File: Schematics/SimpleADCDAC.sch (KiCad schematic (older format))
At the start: 65 parts

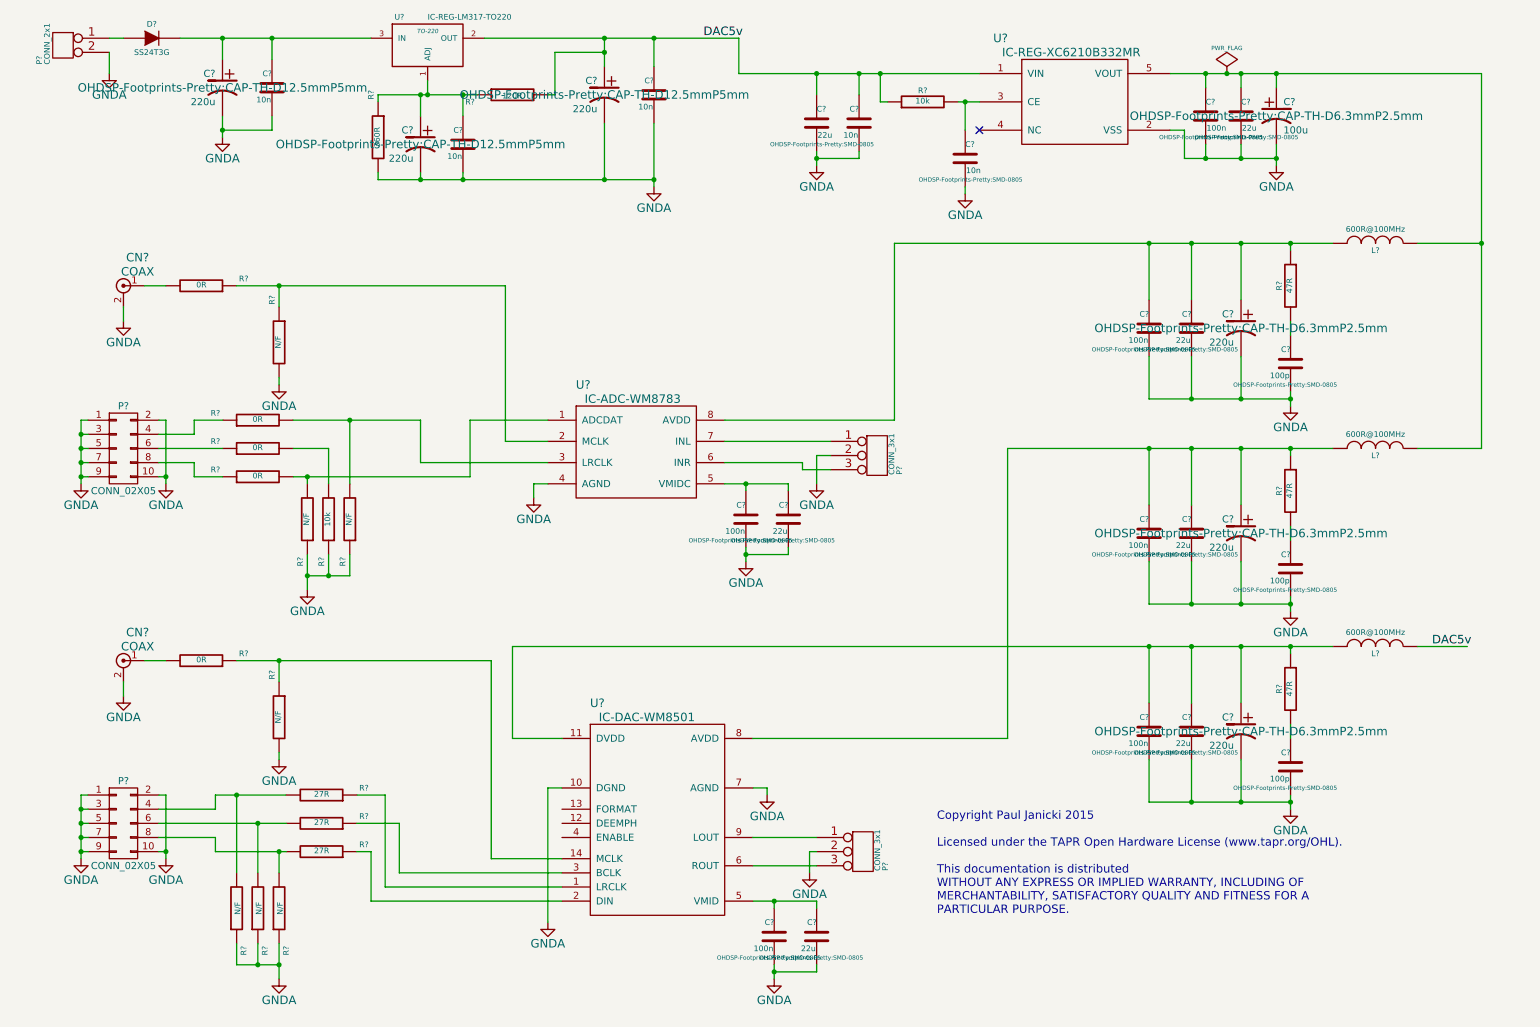
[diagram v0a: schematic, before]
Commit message: Adding ADC/DAC
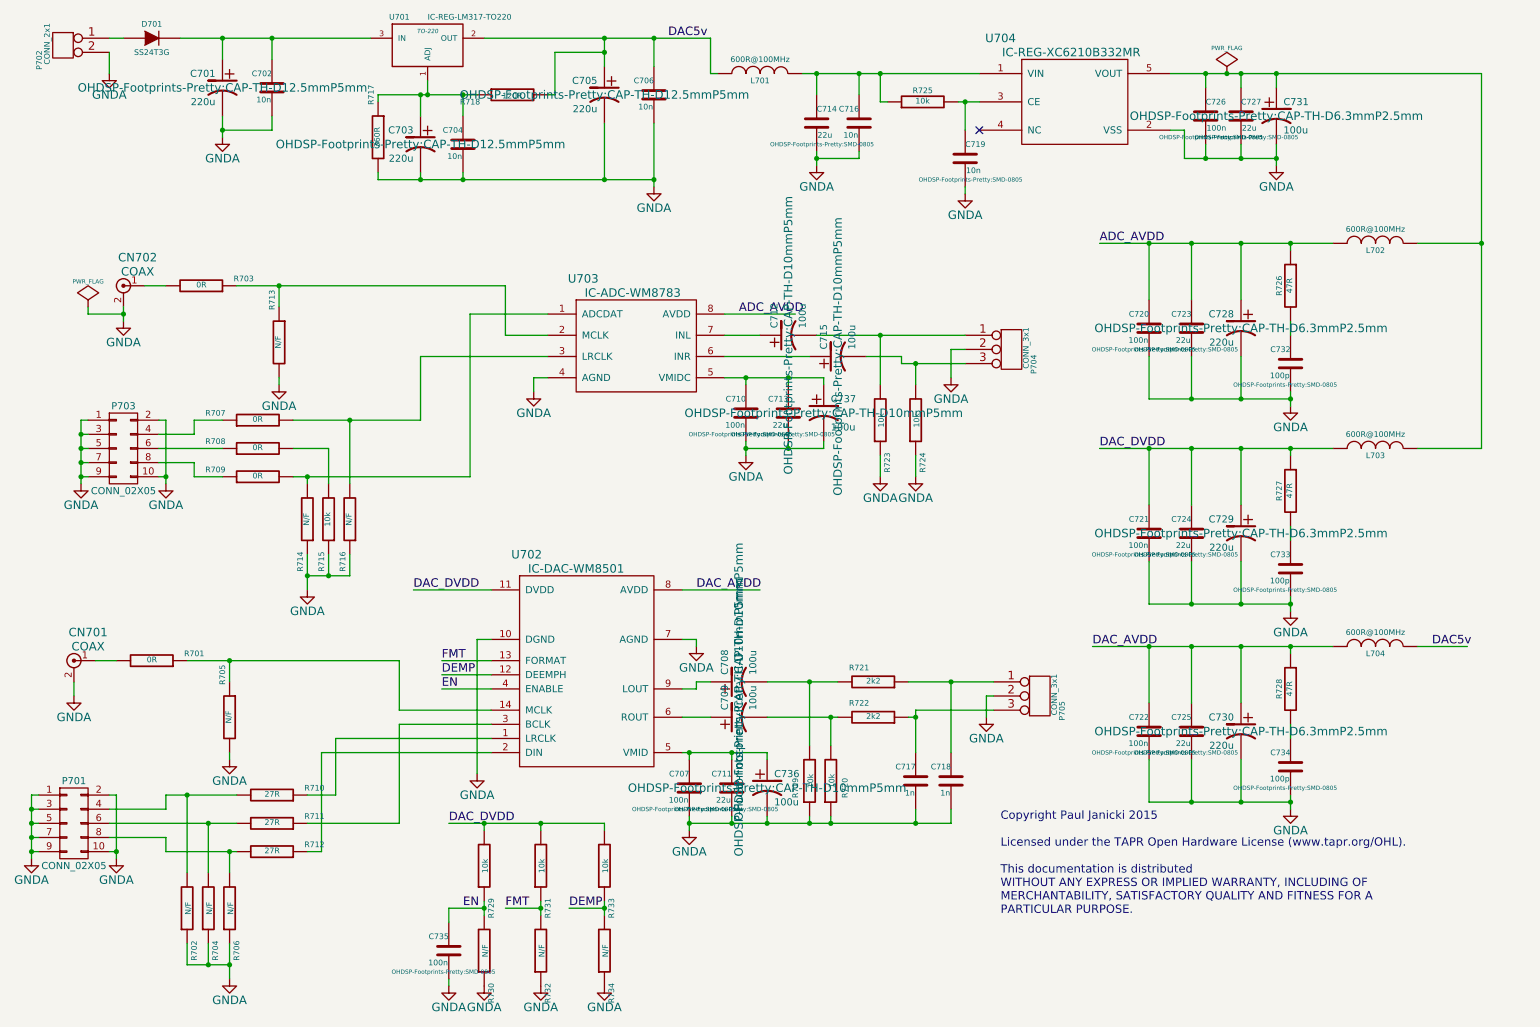
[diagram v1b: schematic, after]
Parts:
- added C708, C709, C712, C715, C736, C737: 100u, OHDSP-Footprints-Pretty:CAP-TH-D10mmP5mm, symbol CP1
- added C717, C718: 1n, symbol C
- added C735: 100n, OHDSP-Footprints-Pretty:SMD-0805, symbol C
- added L701: 600R@100MHz, OHDSP-Footprints-Pretty:SMD-0805, symbol INDUCTOR
- added R719, R720, R723, R724, R729, R731, R733: 10k, OHDSP-Footprints-Pretty:SMD-0603, symbol R
- added R721, R722: 2k2, OHDSP-Footprints-Pretty:SMD-0603, symbol R
- added R730, R732, R734: N/F, OHDSP-Footprints-Pretty:SMD-0603, symbol R
- gave numbers to parts that had none: 65
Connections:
- net DAC5v: now also L701.2; no longer C714.1, C716.1, R725.1, U704.1 (VIN)
- net GNDA: now also C717.2, C718.2, C735.2, C736.2, C737.2, R719.1, R720.1, R723.1, R724.1, R730.1, R732.1, R734.1
- net at C710.1, C713.1, U703.5 (VMIDC): now also C737.1
- net at U703.6 (INR): now also C715.1; no longer P704.3 (P3)
- net at U703.7 (INL): now also C712.1; no longer P704.1 (P1)
- net ADC_AVDD: now reaches C720.1, C723.1, C728.1, L702.2, R726.1, U703.8 (AVDD)
- net DAC_AVDD: now reaches C722.1, C725.1, C730.1, L704.2, R728.1
- net DAC_AVDD: now also U702.8 (AVDD); no longer U702.11 (DVDD)
- net DEMP: now reaches U702.12 (DEEMPH)
- net DEMP: now also R733.1, R734.2
- net FMT: now reaches U702.13 (FORMAT)
- net FMT: now also R731.1, R732.2
- net EN: now reaches U702.4 (ENABLE)
- net EN: now also C735.1, R729.1, R730.2
- net at C707.1, C711.1, U702.5 (VMID): now also C736.1
- net at U702.6 (ROUT): now also C709.1; no longer P705.3 (P3)
- net DAC_DVDD: now reaches C721.1, C724.1, C729.1, L703.2, R727.1
- net DAC_DVDD: now also U702.11 (DVDD), R729.2, R731.2, R733.2; no longer U702.8 (AVDD)
- net at U702.9 (LOUT): now also C708.1; no longer P705.1 (P1)
- new net: C714.1, C716.1, L701.1, R725.1, U704.1 (VIN)
- new net: C708.2, R719.2, R721.2
- new net: C709.2, R720.2, R722.2
- new net: C718.1, P705.1 (P1), R721.1
- new net: C717.1, P705.3 (P3), R722.1
- new net: C712.2, P704.1 (P1), R723.2
- new net: C715.2, P704.3 (P3), R724.2
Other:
- moved on the sheet: C707, C710, C711, C713, CN701, P701, P704, P705, R701, R702, R704, R705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

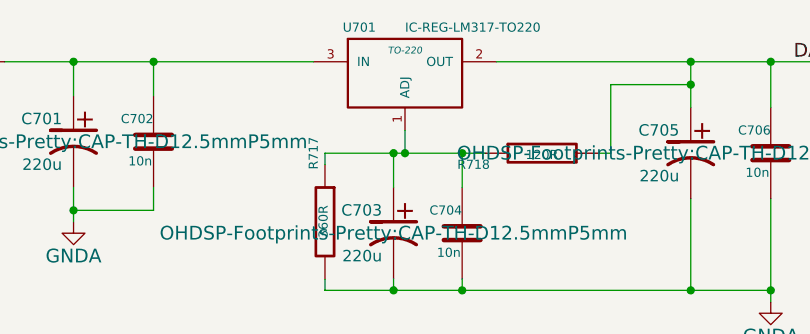
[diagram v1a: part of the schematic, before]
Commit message: Adding DAC/ADC
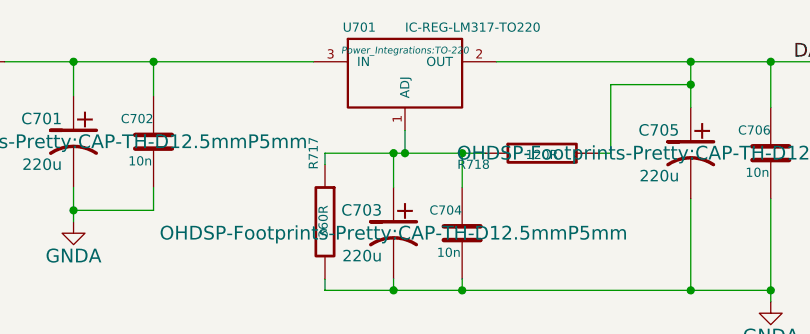
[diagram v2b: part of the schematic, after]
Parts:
- C702, C704, C706, C716, C717, C718: footprint (none) -> OHDSP-Footprints-Pretty:CAP_TH_5mm
- P704, P705: footprint (none) -> OHDSP-Footprints-Pretty:CONN_SIL_3
- R702, R704, R706, R707, R708, R709, R710, R711, R712, R714, R715, R716, R719, R720, R721, R722, R723, R724, R729, R730, R731, R732, R733, R734: footprint OHDSP-Footprints-Pretty:SMD-0603 -> OHDSP-Footprints-Pretty:SMD-0805
- U701: footprint TO-220 -> Power_Integrations:TO-220
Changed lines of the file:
@@
 F 0 "U703" H 4500 3100 60  0000 C CNN
 F 1 "IC-ADC-WM8783" H 4850 3000 60  0000 C CNN
-F 2 "" H 4250 2850 60  0000 C CNN
+F 2 "" H 4250 2850 60  0001 C CNN
 F 3 "" H 4250 2850 60  0000 C CNN
 	1    4250 2850
@@
 F 0 "U702" H 4100 5050 60  0000 C CNN
 F 1 "IC-DAC-WM8501" H 4450 4950 60  0000 C CNN
-F 2 "" H 6250 5150 60  0000 C CNN
+F 2 "" H 6250 5150 60  0001 C CNN
 F 3 "" H 6250 5150 60  0000 C CNN
 	1    3850 4800
@@
 F 0 "R714" V 2600 4600 40  0000 C CNN
 F 1 "N/F" V 2557 4301 40  0000 C CNN
-F 2 "OHDSP-Footprints-Pretty:SMD-0603" V 2480 4300 30  0001 C CNN
+F 2 "OHDSP-Footprints-Pretty:SMD-0805" V 2480 4300 30  0001 C CNN
 F 3 "~" H 2550 4300 30  0000 C CNN
 	1    2550 4300
@@
 F 0 "R715" V 2750 4600 40  0000 C CNN
 F 1 "10k" V 2707 4301 40  0000 C CNN
-F 2 "OHDSP-Footprints-Pretty:SMD-0603" V 2630 4300 30  0001 C CNN
+F 2 "OHDSP-Footprints-Pretty:SMD-0805" V 2630 4300 30  0001 C CNN
 F 3 "~" H 2700 4300 30  0000 C CNN
 	1    2700 4300
@@
 F 0 "R716" V 2900 4600 40  0000 C CNN
 F 1 "N/F" V 2857 4301 40  0000 C CNN
-F 2 "OHDSP-Footprints-Pretty:SMD-0603" V 2780 4300 30  0001 C CNN
+F 2 "OHDSP-Footprints-Pretty:SMD-0805" V 2780 4300 30  0001 C CNN
 F 3 "~" H 2850 4300 30  0000 C CNN
 	1    2850 4300
@@
 F 0 "R707" V 2250 3900 40  0000 C CNN
 F 1 "0R" V 2207 3601 40  0000 C CNN
-F 2 "OHDSP-Footprints-Pretty:SMD-0603" V 2130 3600 30  0001 C CNN
+F 2 "OHDSP-Footprints-Pretty:SMD-0805" V 2130 3600 30  0001 C CNN
 F 3 "~" H 2200 3600 30  0000 C CNN
 	1    2200 3600
@@
 F 0 "R708" V 2250 4100 40  0000 C CNN
 F 1 "0R" V 2207 3801 40  0000 C CNN
-F 2 "OHDSP-Footprints-Pretty:SMD-0603" V 2130 3800 30  0001 C CNN
+F 2 "OHDSP-Footprints-Pretty:SMD-0805" V 2130 3800 30  0001 C CNN
 F 3 "~" H 2200 3800 30  0000 C CNN
 	1    2200 3800
@@
 F 0 "R709" V 2250 4300 40  0000 C CNN
 F 1 "0R" V 2207 4001 40  0000 C CNN
-F 2 "OHDSP-Footprints-Pretty:SMD-0603" V 2130 4000 30  0001 C CNN
+F 2 "OHDSP-Footprints-Pretty:SMD-0805" V 2130 4000 30  0001 C CNN
 F 3 "~" H 2200 4000 30  0000 C CNN
 	1    2200 4000
@@
 F 0 "R710" V 2350 6550 40  0000 C CNN
 F 1 "27R" V 2307 6251 40  0000 C CNN
-F 2 "OHDSP-Footprints-Pretty:SMD-0603" V 2230 6250 30  0001 C CNN
+F 2 "OHDSP-Footprints-Pretty:SMD-0805" V 2230 6250 30  0001 C CNN
 F 3 "~" H 2300 6250 30  0000 C CNN
 	1    2300 6250
@@
 F 0 "R706" V 2050 7350 40  0000 C CNN
 F 1 "N/F" V 2007 7051 40  0000 C CNN
-F 2 "OHDSP-Footprints-Pretty:SMD-0603" V 1930 7050 30  0001 C CNN
+F 2 "OHDSP-Footprints-Pretty:SMD-0805" V 1930 7050 30  0001 C CNN
 F 3 "~" H 2000 7050 30  0000 C CNN
 	1    2000 7050
@@
 F 0 "R704" V 1900 7350 40  0000 C CNN
 F 1 "N/F" V 1857 7051 40  0000 C CNN
-F 2 "OHDSP-Footprints-Pretty:SMD-0603" V 1780 7050 30  0001 C CNN
+F 2 "OHDSP-Footprints-Pretty:SMD-0805" V 1780 7050 30  0001 C CNN
 F 3 "~" H 1850 7050 30  0000 C CNN
 	1    1850 7050
@@
 F 0 "R702" V 1750 7350 40  0000 C CNN
 F 1 "N/F" V 1707 7051 40  0000 C CNN
-F 2 "OHDSP-Footprints-Pretty:SMD-0603" V 1630 7050 30  0001 C CNN
+F 2 "OHDSP-Footprints-Pretty:SMD-0805" V 1630 7050 30  0001 C CNN
 F 3 "~" H 1700 7050 30  0000 C CNN
 	1    1700 7050
@@
 F 0 "R711" V 2350 6750 40  0000 C CNN
 F 1 "27R" V 2307 6451 40  0000 C CNN
-F 2 "OHDSP-Footprints-Pretty:SMD-0603" V 2230 6450 30  0001 C CNN
+F 2 "OHDSP-Footprints-Pretty:SMD-0805" V 2230 6450 30  0001 C CNN
 F 3 "~" H 2300 6450 30  0000 C CNN
 	1    2300 6450
@@
 F 0 "R712" V 2350 6950 40  0000 C CNN
 F 1 "27R" V 2307 6651 40  0000 C CNN
-F 2 "OHDSP-Footprints-Pretty:SMD-0603" V 2230 6650 30  0001 C CNN
+F 2 "OHDSP-Footprints-Pretty:SMD-0805" V 2230 6650 30  0001 C CNN
 F 3 "~" H 2300 6650 30  0000 C CNN
 	1    2300 6650
@@
 F 0 "U701" H 3200 1150 40  0000 C CNN
 F 1 "IC-REG-LM317-TO220" H 3400 1150 40  0000 L CNN
-F 2 "TO-220" H 3400 1050 30  0000 C CIN
+F 2 "Power_Integrations:TO-220" H 3400 1050 30  0000 C CIN
 F 3 "" H 3400 950 60  0000 C CNN
 	1    3400 950
@@
 F 0 "C702" H 2300 1350 40  0000 L CNN
 F 1 "10n" H 2306 1165 40  0000 L CNN
-F 2 "" H 2338 1100 30  0000 C CNN
+F 2 "OHDSP-Footprints-Pretty:CAP_TH_5mm" H 2338 1100 30  0001 C CNN
 F 3 "~" H 2300 1250 60  0000 C CNN
 	1    2300 1250
@@
 F 0 "C706" H 5000 1400 40  0000 L CNN
 F 1 "10n" H 5006 1215 40  0000 L CNN
-F 2 "" H 5038 1150 30  0000 C CNN
+F 2 "OHDSP-Footprints-Pretty:CAP_TH_5mm" H 5038 1150 30  0001 C CNN
 F 3 "~" H 5000 1300 60  0000 C CNN
 	1    5000 1300
@@
 F 0 "C704" H 3650 1750 40  0000 L CNN
 F 1 "10n" H 3656 1565 40  0000 L CNN
-F 2 "" H 3688 1500 30  0000 C CNN
+F 2 "OHDSP-Footprints-Pretty:CAP_TH_5mm" H 3688 1500 30  0001 C CNN
 F 3 "~" H 3650 1650 60  0000 C CNN
 	1    3650 1650
@@
 F 0 "C716" H 6450 1600 40  0000 L CNN
 F 1 "10n" H 6456 1415 40  0000 L CNN
-F 2 "" H 6488 1350 30  0000 C CNN
+F 2 "OHDSP-Footprints-Pretty:CAP_TH_5mm" H 6488 1350 30  0001 C CNN
 F 3 "~" H 6450 1500 60  0000 C CNN
 	1    6450 1500
@@
 F 0 "P704" V 7685 2795 40  0000 C CNN
 F 1 "CONN_3x1" V 7630 2910 40  0000 C CNN
-F 2 "" H 7540 2890 60  0000 C CNN
+F 2 "OHDSP-Footprints-Pretty:CONN_SIL_3" H 7540 2890 60  0001 C CNN
 F 3 "" H 7540 2890 60  0000 C CNN
 	1    7200 3000
@@
 F 0 "P705" V 7885 5245 40  0000 C CNN
 F 1 "CONN_3x1" V 7830 5360 40  0000 C CNN
-F 2 "" H 7740 5340 60  0000 C CNN
+F 2 "OHDSP-Footprints-Pretty:CONN_SIL_3" H 7740 5340 60  0001 C CNN
 F 3 "" H 7740 5340 60  0000 C CNN
 	1    7400 5450
@@
 F 0 "R721" V 6650 5350 40  0000 C CNN
 F 1 "2k2" V 6557 5451 40  0000 C CNN
-F 2 "OHDSP-Footprints-Pretty:SMD-0603" V 6480 5450 30  0001 C CNN
+F 2 "OHDSP-Footprints-Pretty:SMD-0805" V 6480 5450 30  0001 C CNN
 F 3 "~" H 6550 5450 30  0000 C CNN
 	1    6550 5450
@@
 F 0 "R722" V 6650 5600 40  0000 C CNN
 F 1 "2k2" V 6557 5701 40  0000 C CNN
-F 2 "OHDSP-Footprints-Pretty:SMD-0603" V 6480 5700 30  0001 C CNN
+F 2 "OHDSP-Footprints-Pretty:SMD-0805" V 6480 5700 30  0001 C CNN
 F 3 "~" H 6550 5700 30  0000 C CNN
 	1    6550 5700
@@
 F 0 "R719" V 6000 6200 40  0000 C CNN
 F 1 "10k" V 6107 6151 40  0000 C CNN
-F 2 "OHDSP-Footprints-Pretty:SMD-0603" V 6030 6150 30  0001 C CNN
+F 2 "OHDSP-Footprints-Pretty:SMD-0805" V 6030 6150 30  0001 C CNN
 F 3 "~" H 6100 6150 30  0000 C CNN
 	1    6100 6150
@@
 F 0 "R720" V 6350 6200 40  0000 C CNN
 F 1 "10k" V 6257 6151 40  0000 C CNN
-F 2 "OHDSP-Footprints-Pretty:SMD-0603" V 6180 6150 30  0001 C CNN
+F 2 "OHDSP-Footprints-Pretty:SMD-0805" V 6180 6150 30  0001 C CNN
 F 3 "~" H 6250 6150 30  0000 C CNN
 	1    6250 6150
@@
 F 0 "C717" H 6850 6250 40  0000 L CNN
 F 1 "1n" H 6856 6065 40  0000 L CNN
-F 2 "" H 6888 6000 30  0000 C CNN
+F 2 "OHDSP-Footprints-Pretty:CAP_TH_5mm" H 6888 6000 30  0001 C CNN
 F 3 "~" H 6850 6150 60  0000 C CNN
 	1    6850 6150
@@
 F 0 "C718" H 7100 6250 40  0000 L CNN
 F 1 "1n" H 7106 6065 40  0000 L CNN
-F 2 "" H 7138 6000 30  0000 C CNN
+F 2 "OHDSP-Footprints-Pretty:CAP_TH_5mm" H 7138 6000 30  0001 C CNN
 F 3 "~" H 7100 6150 60  0000 C CNN
 	1    7100 6150
@@
 F 0 "R723" V 6650 3900 40  0000 C CNN
 F 1 "10k" V 6607 3601 40  0000 C CNN
-F 2 "OHDSP-Footprints-Pretty:SMD-0603" V 6530 3600 30  0001 C CNN
+F 2 "OHDSP-Footprints-Pretty:SMD-0805" V 6530 3600 30  0001 C CNN
 F 3 "~" H 6600 3600 30  0000 C CNN
 	1    6600 3600
@@
 F 0 "R724" V 6900 3900 40  0000 C CNN
 F 1 "10k" V 6857 3601 40  0000 C CNN
-F 2 "OHDSP-Footprints-Pretty:SMD-0603" V 6780 3600 30  0001 C CNN
+F 2 "OHDSP-Footprints-Pretty:SMD-0805" V 6780 3600 30  0001 C CNN
 F 3 "~" H 6850 3600 30  0000 C CNN
 	1    6850 3600
@@
 F 0 "R729" V 3850 7050 40  0000 C CNN
 F 1 "10k" V 3807 6751 40  0000 C CNN
-F 2 "OHDSP-Footprints-Pretty:SMD-0603" V 3730 6750 30  0001 C CNN
+F 2 "OHDSP-Footprints-Pretty:SMD-0805" V 3730 6750 30  0001 C CNN
 F 3 "~" H 3800 6750 30  0000 C CNN
 	1    3800 6750
@@
 F 0 "R730" V 3850 7650 40  0000 C CNN
 F 1 "N/F" V 3807 7351 40  0000 C CNN
-F 2 "OHDSP-Footprints-Pretty:SMD-0603" V 3730 7350 30  0001 C CNN
+F 2 "OHDSP-Footprints-Pretty:SMD-0805" V 3730 7350 30  0001 C CNN
 F 3 "~" H 3800 7350 30  0000 C CNN
 	1    3800 7350
@@
 F 0 "R731" V 4250 7050 40  0000 C CNN
 F 1 "10k" V 4207 6751 40  0000 C CNN
-F 2 "OHDSP-Footprints-Pretty:SMD-0603" V 4130 6750 30  0001 C CNN
+F 2 "OHDSP-Footprints-Pretty:SMD-0805" V 4130 6750 30  0001 C CNN
 F 3 "~" H 4200 6750 30  0000 C CNN
 	1    4200 6750
@@
 F 0 "R732" V 4250 7650 40  0000 C CNN
 F 1 "N/F" V 4207 7351 40  0000 C CNN
-F 2 "OHDSP-Footprints-Pretty:SMD-0603" V 4130 7350 30  0001 C CNN
+F 2 "OHDSP-Footprints-Pretty:SMD-0805" V 4130 7350 30  0001 C CNN
 F 3 "~" H 4200 7350 30  0000 C CNN
 	1    4200 7350
@@
 F 0 "R733" V 4700 7050 40  0000 C CNN
 F 1 "10k" V 4657 6751 40  0000 C CNN
-F 2 "OHDSP-Footprints-Pretty:SMD-0603" V 4580 6750 30  0001 C CNN
+F 2 "OHDSP-Footprints-Pretty:SMD-0805" V 4580 6750 30  0001 C CNN
 F 3 "~" H 4650 6750 30  0000 C CNN
 	1    4650 6750
@@
 F 0 "R734" V 4700 7650 40  0000 C CNN
 F 1 "N/F" V 4657 7351 40  0000 C CNN
-F 2 "OHDSP-Footprints-Pretty:SMD-0603" V 4580 7350 30  0001 C CNN
+F 2 "OHDSP-Footprints-Pretty:SMD-0805" V 4580 7350 30  0001 C CNN
 F 3 "~" H 4650 7350 30  0000 C CNN
 	1    4650 7350
